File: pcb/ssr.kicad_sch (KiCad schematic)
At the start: 6 parts, among them Q4 Q_NMOS_DGS, U1 10A SSR

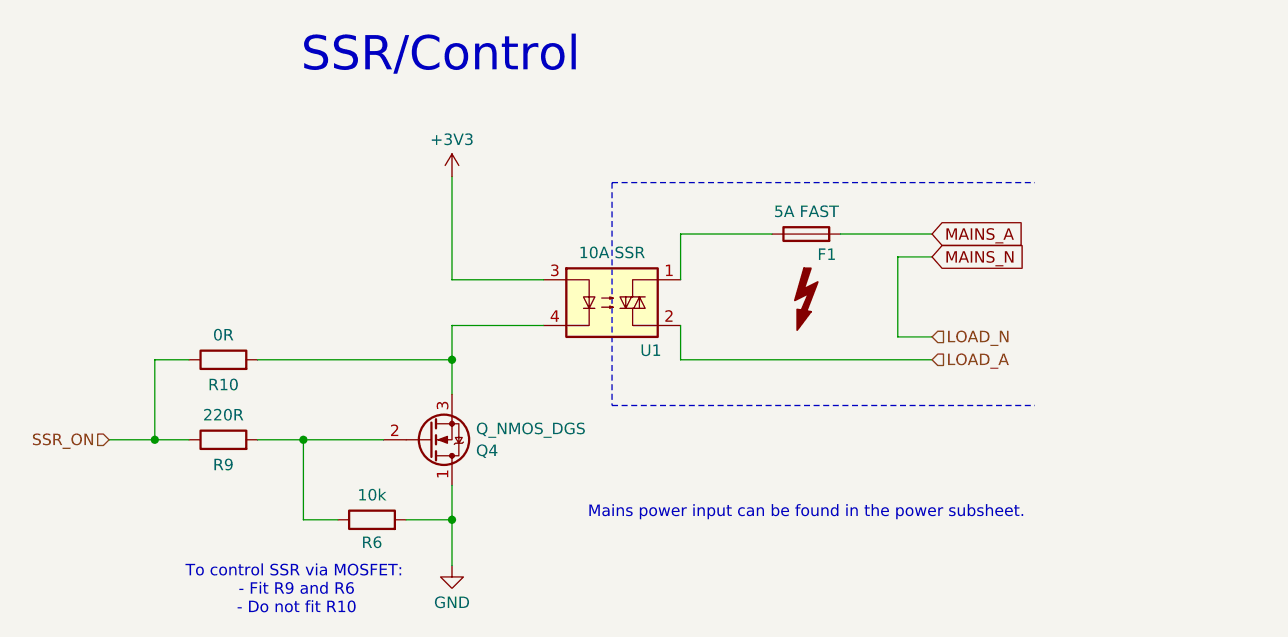
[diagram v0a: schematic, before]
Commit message: Add varistors and other protection components.
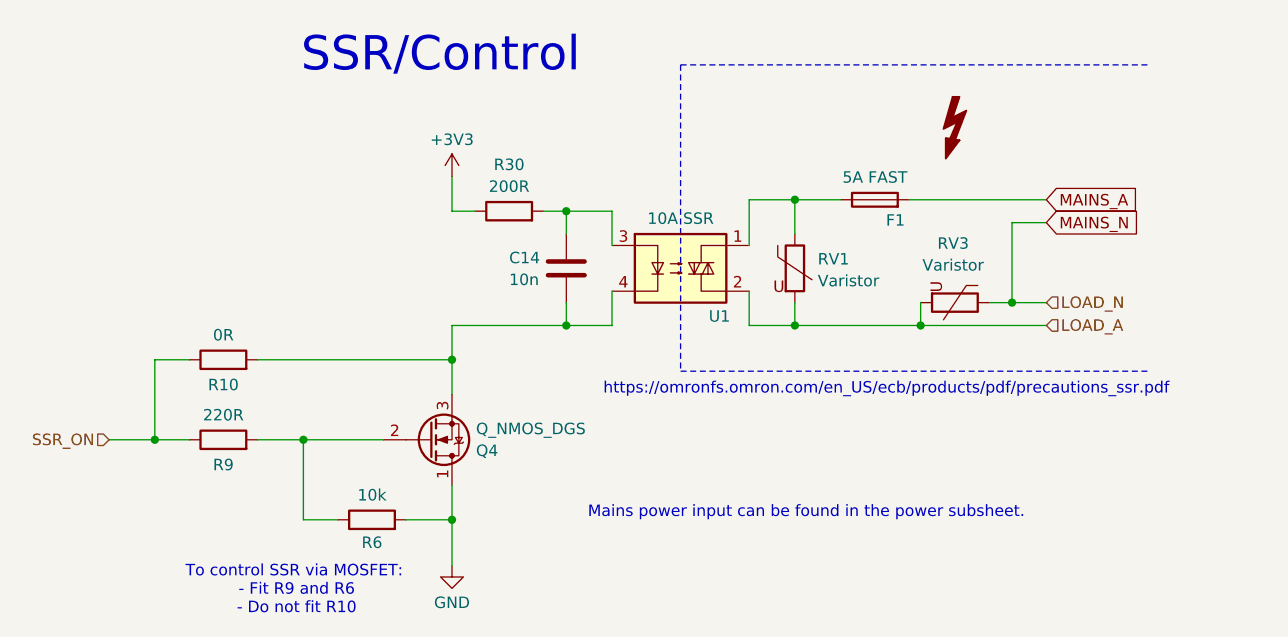
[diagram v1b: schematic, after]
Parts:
- added C14: 10n, symbol Device:C
- added R30: 200R, symbol Device:R
- added RV1, RV3: Varistor, symbol Device:Varistor
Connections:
- net +3V3: now also R30.1; no longer U1.3
- net LOAD_A: now also RV1.2, RV3.2
- net MAINS_N: now also RV3.1
- net at Q4.3 (S), R10.2, U1.4: now also C14.2
- net at F1.1, U1.1: now also RV1.1
- new net: C14.1, R30.2, U1.3
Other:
- note added: "https://omronfs.omron.com/en_US/ecb/products/pdf/precautions_ssr.pdf"
- moved on the sheet: F1, U1
